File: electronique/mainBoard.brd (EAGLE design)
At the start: 63 x 67.5 mm, 32 parts, among them IC1 L298, IC2 7805TV

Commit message: MAJ electronique (final version)
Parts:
- added JP2: (no value), pinhead:1X03
- added LED_LOW_BATT, LED_POWER, LED_STARTING...: (no value), led:LED3MM
- added R4: (no value), resistor:0204/7
- added R5: (no value), resistor:0207/2V
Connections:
- net N$6 renamed MOTOR_EXT
- new net LOW_BATT: LED_LOW_BATT.A, U$1.29
- new net N$7: LED_POWER.K, R4.2
- new net N$9: LED_LOW_BATT.K, LED_STARTING....K, R5.2
- new net STARTING...: LED_STARTING....A, U$1.30
- new net START_SIGNAL: JP2.1, U$1.A11
- net +3V3: now also JP2.2, LED_POWER.A
- net GND: now also JP2.3, R4.1, R5.1
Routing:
- net GPIO0_G: track 43.2 -> 145.5 mm, vias 0 -> 6
- net IN2_DROIT: track 15.8 -> 69.4 mm, vias 0 -> 6
- net SDA: track 307.5 -> 257.2 mm, vias 5 -> 11
- net +3V3: track 331.3 -> 285.6 mm, vias 3 -> 6
- net STARTING...: track 0.00 -> 31.3 mm, vias 0 -> 1
- net LOW_BATT: track 0.00 -> 23.8 mm, vias 0 -> 1
- net GPIO1_AR_D: track 82.4 -> 64.1 mm, vias 4 -> 3
- net START_SIGNAL: track 0.00 -> 18.3 mm
- net GND: track 393.7 -> 375.7 mm, vias 5 -> 9
- net MD_B: track 64.7 -> 47.5 mm, vias 1 -> 3
- net GPIO1_AV_G: track 43.7 -> 27.3 mm, vias 3 -> 0
- net ENABLE_GAUCHE: track 40.0 -> 55.9 mm, vias 1 -> 4
- net N$9: track 0.00 -> 15.8 mm
- net GPIO0_AR_D: track 96.3 -> 111.2 mm, vias 4 -> 3
- net MD_OUT_B: track 30.9 -> 17.8 mm, vias 1 -> 0
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
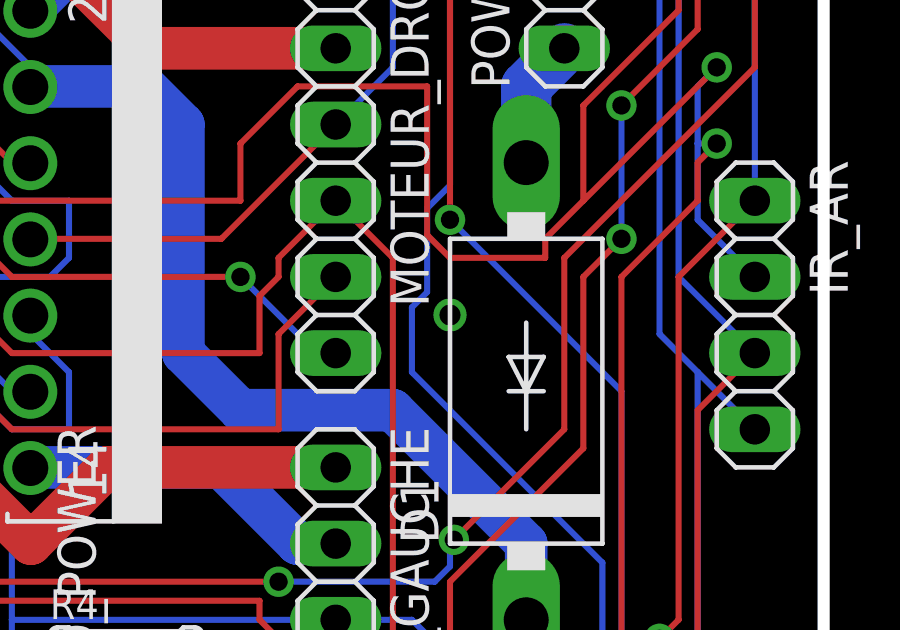
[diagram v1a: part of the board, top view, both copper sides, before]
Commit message: mecanique : mise a jour de la base du robot
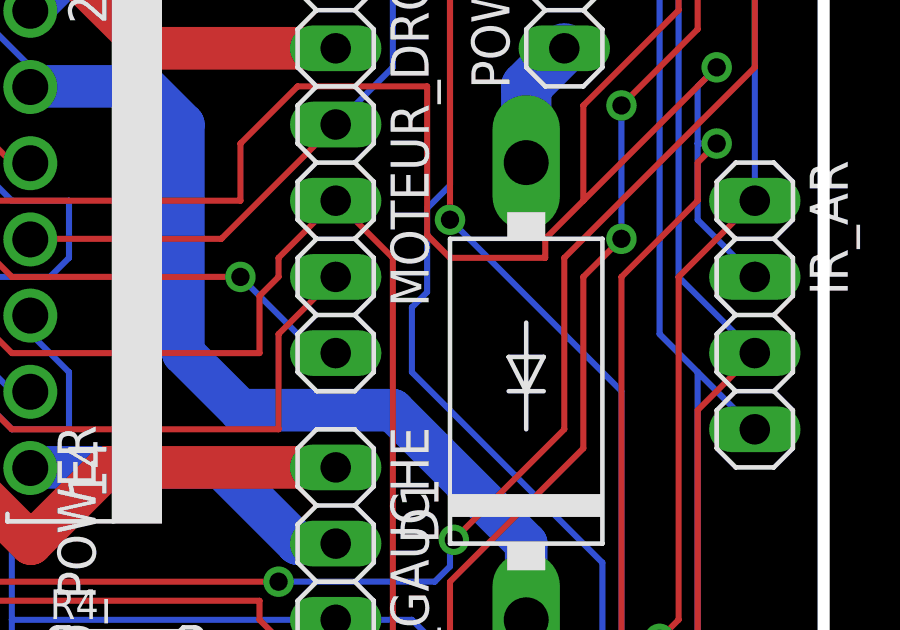
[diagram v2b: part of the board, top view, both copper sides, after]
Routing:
- net GND: vias 9 -> 8
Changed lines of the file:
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@@
 <vertex x="-1.27" y="0"/>
 </polygon>
-<via x="50.8" y="34.29" extent="1-16" drill="0.7"/>
 <via x="46.99" y="49.53" extent="1-16" drill="0.7"/>
 <via x="46.99" y="52.07" extent="1-16" drill="0.7"/>
